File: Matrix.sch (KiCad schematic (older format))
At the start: 171 parts

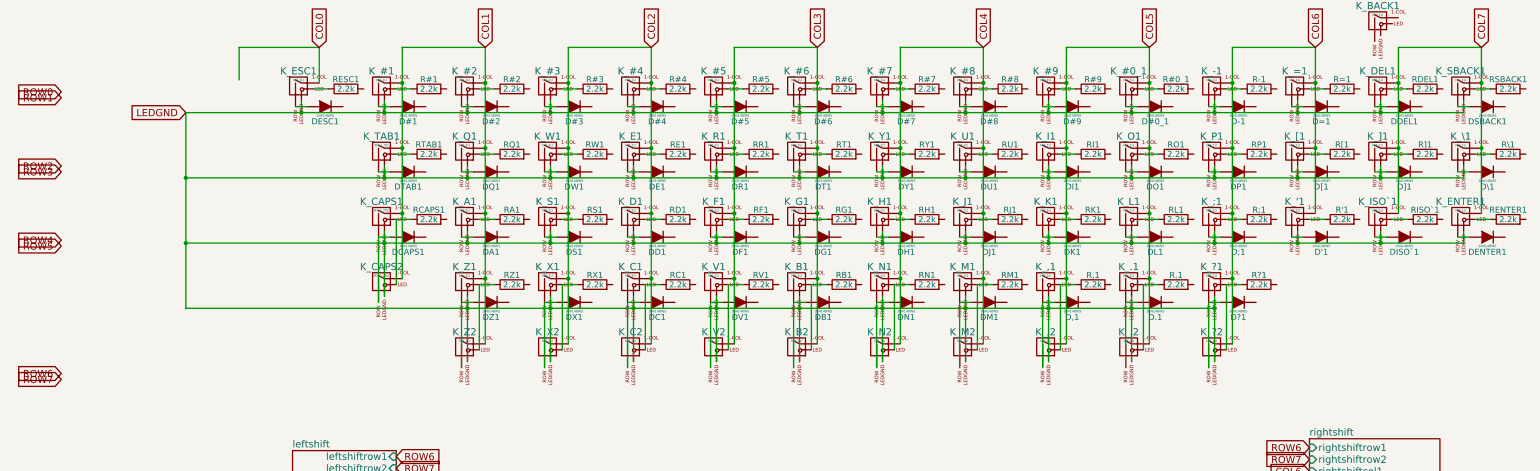
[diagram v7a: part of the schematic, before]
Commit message: Wire rows
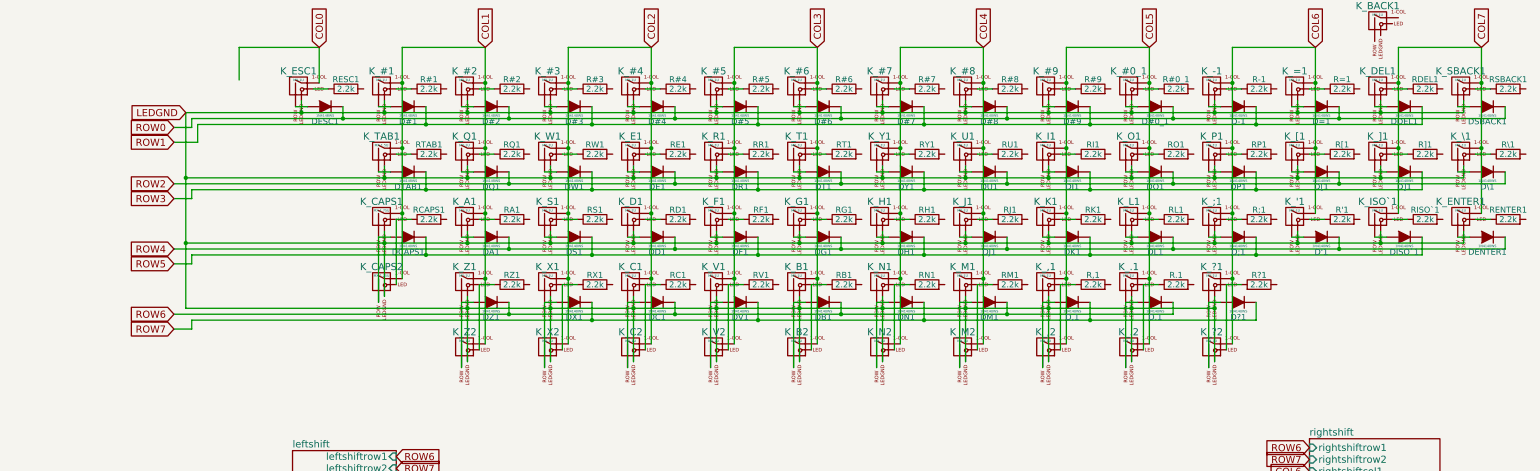
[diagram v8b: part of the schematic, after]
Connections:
- net ROW0: now also D#0_1.1 (K), D#2.1 (K), D#4.1 (K), D#6.1 (K), D#8.1 (K), D=1.1 (K), DESC1.1 (K), DSBACK1.1 (K)
- net ROW1: now also D#1.1 (K), D#3.1 (K), D#5.1 (K), D#7.1 (K), D#9.1 (K), D-1.1 (K), DDEL1.1 (K)
- net ROW2: now also DE1.1 (K), DO1.1 (K), DQ1.1 (K), DT1.1 (K), DU1.1 (K), D[1.1 (K), D\1.1 (K)
- net ROW3: now also DI1.1 (K), DP1.1 (K), DR1.1 (K), DTAB1.1 (K), DW1.1 (K), DY1.1 (K), D]1.1 (K)
- net ROW4: now also D'1.1 (K), DA1.1 (K), DD1.1 (K), DENTER1.1 (K), DG1.1 (K), DJ1.1 (K), DL1.1 (K)
- net ROW5: now also D;1.1 (K), DCAPS1.1 (K), DF1.1 (K), DH1.1 (K), DISO`1.1 (K), DK1.1 (K), DS1.1 (K)
- net ROW6: now also D.1.1 (K), DB1.1 (K), DC1.1 (K), DM1.1 (K), DZ1.1 (K)
- net ROW7: now also D,1.1 (K), D?1.1 (K), DN1.1 (K), DV1.1 (K), DX1.1 (K)
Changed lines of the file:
@@
 	0    -1   -1   0
 $EndComp
-Text GLabel 1300 2625 0    60   Input ~ 0
+Text GLabel 2250 2925 0    60   Input ~ 0
 ROW0
-Text GLabel 1300 2675 0    60   Input ~ 0
+Text GLabel 2250 3050 0    60   Input ~ 0
 ROW1
-Text GLabel 1300 3250 0    60   Input ~ 0
+Text GLabel 2250 3400 0    60   Input ~ 0
 ROW2
-Text GLabel 1300 3300 0    60   Input ~ 0
+Text GLabel 2250 3525 0    60   Input ~ 0
 ROW3
-Text GLabel 1300 3875 0    60   Input ~ 0
+Text GLabel 2250 3950 0    60   Input ~ 0
 ROW4
-Text GLabel 1300 3925 0    60   Input ~ 0
+Text GLabel 2250 4075 0    60   Input ~ 0
 ROW5
-Text GLabel 1300 5000 0    60   Input ~ 0
+Text GLabel 2250 4500 0    60   Input ~ 0
 ROW6
-Text GLabel 1300 5050 0    60   Input ~ 0
+Text GLabel 2250 4625 0    60   Input ~ 0
 ROW7
 Text GLabel 3475 2250 1    60   Input ~ 0
@@
 Connection ~ 2350 3350
 Connection ~ 2350 3900
+Wire Wire Line
+	3675 2750 3675 2850
+Wire Wire Line
+	2400 2850 13475 2850
+Wire Wire Line
+	5075 2850 5075 2750
+Wire Wire Line
+	6475 2850 6475 2750
+Connection ~ 5075 2850
+Wire Wire Line
+	7875 2850 7875 2750
+Connection ~ 6475 2850
+Wire Wire Line
+	9275 2850 9275 2750
+Connection ~ 7875 2850
+Wire Wire Line
+	10675 2850 10675 2750
+Connection ~ 9275 2850
+Wire Wire Line
+	12075 2850 12075 2750
+Connection ~ 10675 2850
+Wire Wire Line
+	13475 2850 13475 2750
+Connection ~ 12075 2850
+Wire Wire Line
+	2400 2850 2400 2925
+Wire Wire Line
+	2400 2925 2250 2925
+Connection ~ 3675 2850
+Wire Wire Line
+	2250 3050 2450 3050
+Wire Wire Line
+	2450 3050 2450 2900
+Wire Wire Line
+	2450 2900 12775 2900
+Wire Wire Line
+	4375 2900 4375 2750
+Wire Wire Line
+	5775 2900 5775 2750
+Connection ~ 4375 2900
+Wire Wire Line
+	7175 2900 7175 2750
+Connection ~ 5775 2900
+Wire Wire Line
+	8575 2900 8575 2750
+Connection ~ 7175 2900
+Wire Wire Line
+	9975 2900 9975 2750
+Connection ~ 8575 2900
+Wire Wire Line
+	11375 2900 11375 2750
+Connection ~ 9975 2900
+Wire Wire Line
+	12775 2900 12775 2750
+Connection ~ 11375 2900
+Wire Wire Line
+	2250 3400 13475 3400
+Wire Wire Line
+	5075 3400 5075 3300
+Wire Wire Line
+	2250 3525 2400 3525
+Wire Wire Line
+	2400 3525 2400 3450
+Wire Wire Line
+	2400 3450 12775 3450
+Wire Wire Line
+	4375 3450 4375 3300
+Wire Wire Line
+	6475 3400 6475 3300
+Connection ~ 5075 3400
+Wire Wire Line
+	7875 3400 7875 3300
+Connection ~ 6475 3400
+Wire Wire Line
+	9275 3400 9275 3300
+Connection ~ 7875 3400
+Wire Wire Line
+	10675 3400 10675 3300
+Connection ~ 9275 3400
+Wire Wire Line
+	12075 3400 12075 3300
+Connection ~ 10675 3400
+Wire Wire Line
+	13475 3400 13475 3300
+Connection ~ 12075 3400
+Wire Wire Line
+	5775 3450 5775 3300
+Connection ~ 4375 3450
+Wire Wire Line
+	7175 3450 7175 3300
+Connection ~ 5775 3450
+Wire Wire Line
+	8575 3450 8575 3300
+Connection ~ 7175 3450
+Wire Wire Line
+	9975 3450 9975 3300
+Connection ~ 8575 3450
+Wire Wire Line
+	11375 3450 11375 3300
+Connection ~ 9975 3450
+Wire Wire Line
+	12775 3450 12775 3300
+Connection ~ 11375 3450
+Wire Wire Line
+	2250 3950 13475 3950
+Wire Wire Line
+	5075 3950 5075 3850
+Wire Wire Line
+	6475 3950 6475 3850
+Connection ~ 5075 3950
+Wire Wire Line
+	7875 3950 7875 3850
+Connection ~ 6475 3950
+Wire Wire Line
+	9275 3950 9275 3850
+Connection ~ 7875 3950
+Wire Wire Line
+	10675 3950 10675 3850
+Connection ~ 9275 3950
+Wire Wire Line
+	12075 3950 12075 3850
+Connection ~ 10675 3950
+Wire Wire Line
+	13475 3950 13475 3850
+Connection ~ 12075 3950
+Wire Wire Line
+	2250 4075 2400 4075
+Wire Wire Line
+	2400 4075 2400 4000
+Wire Wire Line
+	2400 4000 12775 4000
+Wire Wire Line
+	4375 4000 4375 3850
+Wire Wire Line
+	5775 4000 5775 3850
+Connection ~ 4375 4000
+Wire Wire Line
+	7175 4000 7175 3850
+Connection ~ 5775 4000
+Wire Wire Line
+	8575 4000 8575 3850
+Connection ~ 7175 4000
+Wire Wire Line
+	9975 4000 9975 3850
+Connection ~ 8575 4000
+Wire Wire Line
+	11375 4000 11375 3850
+Connection ~ 9975 4000
+Wire Wire Line
+	12775 4000 12775 3850
+Connection ~ 11375 4000
+Wire Wire Line
+	2250 4500 10675 4500
+Wire Wire Line
+	5075 4500 5075 4400
+Wire Wire Line
+	6475 4500 6475 4400
+Connection ~ 5075 4500
+Wire Wire Line
+	7875 4500 7875 4400
+Connection ~ 6475 4500
+Wire Wire Line
+	9275 4500 9275 4400
+Connection ~ 7875 4500
+Wire Wire Line
+	10675 4500 10675 4400
+Connection ~ 9275 4500
+Wire Wire Line
+	2250 4625 2400 4625
+Wire Wire Line
+	2400 4625 2400 4550
+Wire Wire Line
+	2400 4550 11375 4550
+Wire Wire Line
+	5775 4550 5775 4400
+Wire Wire Line
+	7175 4550 7175 4400
+Connection ~ 5775 4550
+Wire Wire Line
+	8575 4550 8575 4400
+Connection ~ 7175 4550
+Wire Wire Line
+	9975 4550 9975 4400
+Connection ~ 8575 4550
+Wire Wire Line
+	11375 4550 11375 4400
+Connection ~ 9975 4550
 $EndSCHEMATC
